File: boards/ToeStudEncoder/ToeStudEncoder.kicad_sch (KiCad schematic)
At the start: 27 parts, among them J1 Swell, J2 ISP, J3 ToeLeft, J4 ToeRight, J5 MIDI In, J8 MIDI Out, J9 Controller, Q1 BC547, U1 ATmega48-20P, U2 6N137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

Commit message: Added bypass caps to power supplies, use cheaper MAX232 IC.
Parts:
- added C3: 330nF, Capacitor_THT:C_Disc_D4.3mm_W1.9mm_P5.00mm, symbol Device:C
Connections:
- net +12V: now also C3.1
- net GND: now also C3.2
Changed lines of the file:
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@@
+	(wire
+		(pts
+			(xy 93.98 161.29) (xy 107.95 161.29)
+		)
+		(stroke
+			(width 0)
+			(type default)
+		)
+	)
 	(wire
 		(pts
@@
 		(pts
 			(xy 187.96 38.1) (xy 191.77 38.1)
+		)
+		(stroke
+			(width 0)
+			(type default)
+		)
+	)
+	(wire
+		(pts
+			(xy 93.98 162.56) (xy 93.98 161.29)
 		)
 		(stroke
@@
 	)
 	(symbol
+		(lib_id "power:GND")
+		(at 93.98 170.18 0)
+		(unit 1)
+		(exclude_from_sim no)
+		(in_bom yes)
+		(on_board yes)
+		(dnp no)
+		(fields_autoplaced yes)
+		(property "Reference" "#PWR013"
+			(at 93.98 176.53 0)
+			(effects
+				(font
+					(size 1.27 1.27)
+				)
+				(hide yes)
+			)
+		)
+		(property "Value" "GND"
+			(at 93.98 175.26 0)
+			(effects
+				(font
+					(size 1.27 1.27)
+				)
+			)
+		)
+		(property "Footprint" ""
+			(at 93.98 170.18 0)
+			(effects
+				(font
+					(size 1.27 1.27)
+				)
+				(hide yes)
+			)
+		)
+		(property "Datasheet" ""
+			(at 93.98 170.18 0)
+			(effects
+				(font
+					(size 1.27 1.27)
+				)
+				(hide yes)
+			)
+		)
+		(property "Description" "Power symbol creates a global label with name \"GND\" , ground"
+			(at 93.98 170.18 0)
+			(effects
+				(font
+					(size 1.27 1.27)
+				)
+				(hide yes)
+			)
+		)
+		(pin "1"
+		)
+		(instances
+			(project "ToeStudEncoder"
+				(path "/a0f642fd-a17d-4032-8879-54d542360da8"
+					(reference "#PWR013")
+					(unit 1)
+				)
+			)
+		)
+	)
+	(symbol
 		(lib_id "Connector_Generic:Conn_02x05_Odd_Even")
 		(at 151.13 106.68 0)
@@
 					(unit 1)
 				)
+			)
+		)
+	)
+	(symbol
+		(lib_id "Device:C")
+		(at 93.98 166.37 0)
+		(unit 1)
+		(exclude_from_sim no)
+		(in_bom yes)
+		(on_board yes)
+		(dnp no)
+		(fields_autoplaced yes)
+		(property "Reference" "C3"
+			(at 97.79 165.0999 0)
+			(effects
+				(font
+					(size 1.27 1.27)
+				)
+				(justify left)
+			)
+		)
+		(property "Value" "330nF"
+			(at 97.79 167.6399 0)
+			(effects
+				(font
+					(size 1.27 1.27)
+				)
+				(justify left)
+			)
+		)
+		(property "Footprint" "Capacitor_THT:C_Disc_D4.3mm_W1.9mm_P5.00mm"
+			(at 94.9452 170.18 0)
+			(effects
+				(font
+					(size 1.27 1.27)
+				)
+				(hide yes)
+			)
+		)
+		(property "Datasheet" "~"
+			(at 93.98 166.37 0)
+			(effects
+				(font
+					(size 1.27 1.27)
+				)
+				(hide yes)
+			)
+		)
+		(property "Description" "Unpolarized capacitor"
+			(at 93.98 166.37 0)
+			(effects
+				(font
+					(size 1.27 1.27)
+				)
+				(hide yes)
+			)
+		)
+		(pin "1"
+		)
+		(pin "2"
+		)
+		(instances
+			(project "ToeStudEncoder"
+				(path "/a0f642fd-a17d-4032-8879-54d542360da8"
+					(reference "C3")
+					(unit 1)
+				)

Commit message: Updated design rules to 0.32mm template and exported Gerber files
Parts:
- R1, R4, R5: footprint Resistor_THT:R_Axial_DIN0204_L3.6mm_D1.6mm_P2.54mm_Vertical -> Resistor_THT:R_Axial_DIN0207_L6.3mm_D2.5mm_P2.54mm_Vertical
- R2: footprint Resistor_THT:R_Axial_DIN0204_L3.6mm_D1.6mm_P7.62mm_Horizontal -> Resistor_THT:R_Axial_DIN0207_L6.3mm_D2.5mm_P2.54mm_Vertical
- R3: footprint Resistor_THT:R_Axial_DIN0204_L3.6mm_D1.6mm_P7.62mm_Horizontal -> Resistor_THT:R_Axial_DIN0207_L6.3mm_D2.5mm_P10.16mm_Horizontal
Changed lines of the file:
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@@
 			)
 		)
-		(property "Footprint" "Resistor_THT:R_Axial_DIN0204_L3.6mm_D1.6mm_P2.54mm_Vertical"
+		(property "Footprint" "Resistor_THT:R_Axial_DIN0207_L6.3mm_D2.5mm_P2.54mm_Vertical"
 			(at 239.268 62.23 90)
 			(effects
@@
 			)
 		)
-		(property "Footprint" "Resistor_THT:R_Axial_DIN0204_L3.6mm_D1.6mm_P7.62mm_Horizontal"
+		(property "Footprint" "Resistor_THT:R_Axial_DIN0207_L6.3mm_D2.5mm_P2.54mm_Vertical"
 			(at 195.58 124.968 90)
 			(effects
@@
 			)
 		)
-		(property "Footprint" "Resistor_THT:R_Axial_DIN0204_L3.6mm_D1.6mm_P2.54mm_Vertical"
+		(property "Footprint" "Resistor_THT:R_Axial_DIN0207_L6.3mm_D2.5mm_P2.54mm_Vertical"
 			(at 231.14 24.892 90)
 			(effects
@@
 			)
 		)
-		(property "Footprint" "Resistor_THT:R_Axial_DIN0204_L3.6mm_D1.6mm_P2.54mm_Vertical"
+		(property "Footprint" "Resistor_THT:R_Axial_DIN0207_L6.3mm_D2.5mm_P2.54mm_Vertical"
 			(at 189.992 30.48 90)
 			(effects
@@
 			)
 		)
-		(property "Footprint" "Resistor_THT:R_Axial_DIN0204_L3.6mm_D1.6mm_P7.62mm_Horizontal"
+		(property "Footprint" "Resistor_THT:R_Axial_DIN0207_L6.3mm_D2.5mm_P10.16mm_Horizontal"
 			(at 231.14 72.898 90)
 			(effects

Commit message: Make Toestud PS2 connectors symmetrical to avoid connection errors
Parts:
- added R6: 220, Resistor_THT:R_Axial_DIN0207_L6.3mm_D2.5mm_P10.16mm_Horizontal, symbol Device:R
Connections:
- net TXD: now also R6.1; no longer J9.4_2
- net at J9.4_1: now also J9.4_2, R6.2
- no-connect marks 16 -> 15
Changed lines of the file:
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@@
 	)
 	(junction
+		(at 215.9 137.16)
+		(diameter 0)
+		(color 0 0 0 0)
+	)
+	(junction
 		(at 157.48 49.53)
 		(diameter 0)
@@
 	)
 	(no_connect
-		(at 215.9 114.3)
-	)
-	(no_connect
 		(at 86.36 115.57)
 	)
@@
 	(wire
 		(pts
+			(xy 212.09 137.16) (xy 215.9 137.16)
+		)
+		(stroke
+			(width 0)
+			(type default)
+		)
+	)
+	(wire
+		(pts
 			(xy 73.66 57.15) (xy 73.66 59.69)
 		)
@@
 	(wire
 		(pts
+			(xy 204.47 137.16) (xy 200.66 137.16)
+		)
+		(stroke
+			(width 0)
+			(type default)
+		)
+	)
+	(wire
+		(pts
 			(xy 93.98 161.29) (xy 107.95 161.29)
 		)
@@
 	(wire
 		(pts
+			(xy 215.9 114.3) (xy 215.9 137.16)
+		)
+		(stroke
+			(width 0)
+			(type default)
+		)
+	)
+	(wire
+		(pts
 			(xy 114.3 85.09) (xy 114.3 87.63)
 		)
@@
 	(global_label "TXD"
 		(shape input)
-		(at 215.9 137.16 180)
+		(at 200.66 137.16 180)
 		(fields_autoplaced yes)
 		(effects
@@
 		)
 		(property "Intersheetrefs" "${INTERSHEET_REFS}"
-			(at 209.4677 137.16 0)
+			(at 194.2277 137.16 0)
 			(effects
 				(font
@@
 					(unit 1)
 				)
+			)
+		)
+	)
+	(symbol
+		(lib_id "Device:R")
+		(at 208.28 137.16 90)
+		(mirror x)
+		(unit 1)
+		(exclude_from_sim no)
+		(in_bom yes)
+		(on_board yes)
+		(dnp no)
+		(property "Reference" "R6"
+			(at 208.28 143.51 90)
+			(effects
+				(font
+					(size 1.27 1.27)
+				)
+			)
+		)
+		(property "Value" "220"
+			(at 208.28 140.97 90)
+			(effects
+				(font
+					(size 1.27 1.27)
+				)
+			)
+		)
+		(property "Footprint" "Resistor_THT:R_Axial_DIN0207_L6.3mm_D2.5mm_P10.16mm_Horizontal"
+			(at 208.28 135.382 90)
+			(effects
+				(font
+					(size 1.27 1.27)
+				)
+				(hide yes)
+			)
+		)
+		(property "Datasheet" "~"
+			(at 208.28 137.16 0)
+			(effects
+				(font
+					(size 1.27 1.27)
+				)
+				(hide yes)
+			)
+		)
+		(property "Description" "Resistor"
+			(at 208.28 137.16 0)
+			(effects
+				(font
+					(size 1.27 1.27)
+				)
+				(hide yes)
+			)
+		)
+		(pin "1"
+		)
+		(pin "2"
+		)
+		(instances
+			(project "ToeStudEncoder"
+				(path "/a0f642fd-a17d-4032-8879-54d542360da8"
+					(reference "R6")
+					(unit 1)
+				)

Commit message: ToeStudEncoder: Fixed mirrored PS2 pinout
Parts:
- R4: footprint Resistor_THT:R_Axial_DIN0207_L6.3mm_D2.5mm_P2.54mm_Vertical -> Resistor_THT:R_Axial_DIN0207_L6.3mm_D2.5mm_P10.16mm_Horizontal
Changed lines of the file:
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@@
 			)
 		)
-		(property "Footprint" "Resistor_THT:R_Axial_DIN0207_L6.3mm_D2.5mm_P2.54mm_Vertical"
+		(property "Footprint" "Resistor_THT:R_Axial_DIN0207_L6.3mm_D2.5mm_P10.16mm_Horizontal"
 			(at 239.268 62.23 90)
 			(effects

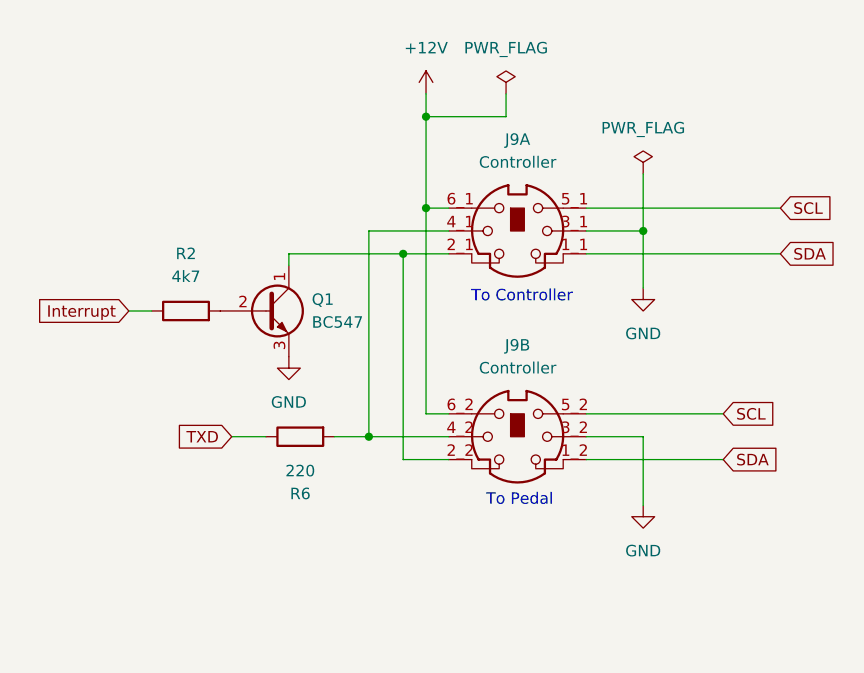
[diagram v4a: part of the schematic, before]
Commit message: Disconnected UART lines to avoid interference
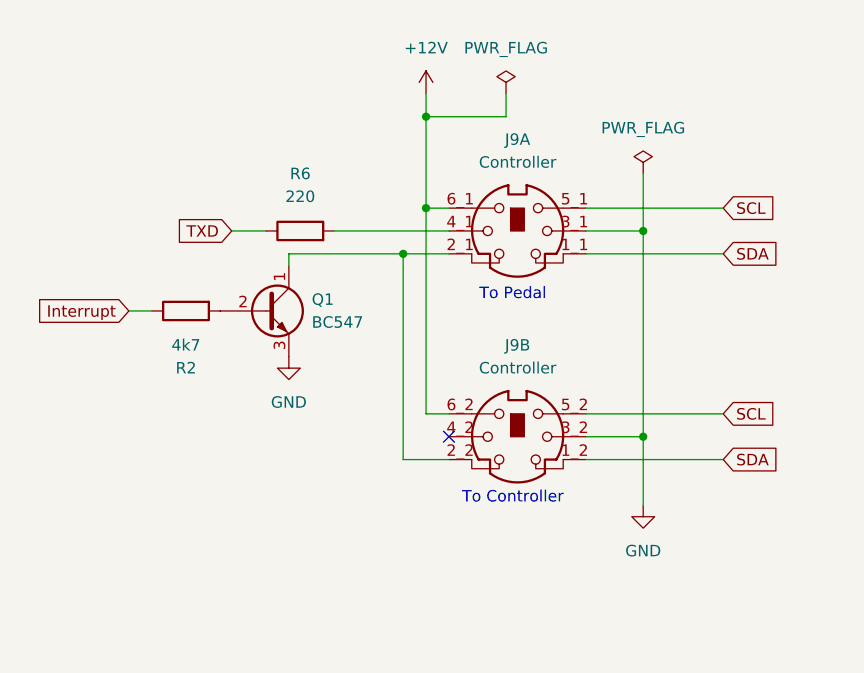
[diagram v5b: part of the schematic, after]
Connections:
- net at J9.4_1, R6.2: no longer J9.4_2
- no-connect marks 15 -> 16
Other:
- moved on the sheet: R6
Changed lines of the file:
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@@
 	)
 	(junction
-		(at 215.9 137.16)
-		(diameter 0)
-		(color 0 0 0 0)
-	)
-	(junction
 		(at 157.48 49.53)
 		(diameter 0)
@@
 	)
 	(junction
+		(at 246.38 137.16)
+		(diameter 0)
+		(color 0 0 0 0)
+	)
+	(junction
 		(at 162.56 111.76)
 		(diameter 0)
@@
 	)
 	(no_connect
+		(at 224.79 137.16)
+	)
+	(no_connect
 		(at 86.36 115.57)
 	)
@@
 	(wire
 		(pts
-			(xy 224.79 114.3) (xy 215.9 114.3)
-		)
-		(stroke
-			(width 0)
-			(type default)
-		)
-	)
-	(wire
-		(pts
 			(xy 240.03 139.7) (xy 255.27 139.7)
 		)
@@
 	(wire
 		(pts
-			(xy 71.12 135.89) (xy 71.12 139.7)
+			(xy 246.38 114.3) (xy 246.38 137.16)
 		)
 		(stroke
@@
 	(wire
 		(pts
-			(xy 157.48 39.37) (xy 157.48 35.56)
+			(xy 71.12 135.89) (xy 71.12 139.7)
 		)
 		(stroke
@@
 	(wire
 		(pts
-			(xy 219.71 139.7) (xy 224.79 139.7)
+			(xy 157.48 39.37) (xy 157.48 35.56)
 		)
 		(stroke
@@
 	(wire
 		(pts
-			(xy 212.09 137.16) (xy 215.9 137.16)
+			(xy 219.71 139.7) (xy 224.79 139.7)
 		)
 		(stroke
@@
 	(wire
 		(pts
-			(xy 246.38 114.3) (xy 246.38 120.65)
-		)
-		(stroke
-			(width 0)
-			(type default)
-		)
-	)
-	(wire
-		(pts
 			(xy 234.95 71.12) (xy 240.03 71.12)
 		)
@@
 	(wire
 		(pts
-			(xy 204.47 137.16) (xy 200.66 137.16)
+			(xy 204.47 114.3) (xy 200.66 114.3)
 		)
 		(stroke
@@
 	(wire
 		(pts
-			(xy 215.9 137.16) (xy 224.79 137.16)
+			(xy 212.09 114.3) (xy 224.79 114.3)
 		)
 		(stroke
@@
 	(wire
 		(pts
-			(xy 240.03 111.76) (xy 261.62 111.76)
+			(xy 240.03 111.76) (xy 255.27 111.76)
 		)
 		(stroke
@@
 	(wire
 		(pts
-			(xy 215.9 114.3) (xy 215.9 137.16)
-		)
-		(stroke
-			(width 0)
-			(type default)
-		)
-	)
-	(wire
-		(pts
 			(xy 114.3 85.09) (xy 114.3 87.63)
 		)
@@
 	(wire
 		(pts
-			(xy 240.03 116.84) (xy 261.62 116.84)
+			(xy 240.03 116.84) (xy 255.27 116.84)
 		)
 		(stroke
@@
 	(text "To Controller"
 		(exclude_from_sim no)
-		(at 232.918 121.666 0)
+		(at 231.902 144.018 0)
 		(effects
 			(font
@@
 	(text "To Pedal"
 		(exclude_from_sim no)
-		(at 232.664 144.272 0)
+		(at 231.902 121.412 0)
 		(effects
 			(font
@@
 	(global_label "SDA"
 		(shape input)
-		(at 261.62 116.84 0)
+		(at 255.27 116.84 0)
 		(fields_autoplaced yes)
 		(effects
@@
 		)
 		(property "Intersheetrefs" "${INTERSHEET_REFS}"
-			(at 267.6012 116.7606 0)
+			(at 261.2512 116.7606 0)
 			(effects
 				(font
@@
 	(global_label "TXD"
 		(shape input)
-		(at 200.66 137.16 180)
+		(at 200.66 114.3 180)
 		(fields_autoplaced yes)
 		(effects
@@
 		)
 		(property "Intersheetrefs" "${INTERSHEET_REFS}"
-			(at 194.2277 137.16 0)
+			(at 194.2277 114.3 0)
 			(effects
 				(font
@@
 	(global_label "SCL"
 		(shape input)
-		(at 261.62 111.76 0)
+		(at 255.27 111.76 0)
 		(fields_autoplaced yes)
 		(effects
@@
 		)
 		(property "Intersheetrefs" "${INTERSHEET_REFS}"
-			(at 267.5407 111.6806 0)
+			(at 261.1907 111.6806 0)
 			(effects
 				(font
@@
 		(lib_id "Device:R")
 		(at 195.58 123.19 90)
+		(mirror x)
 		(unit 1)
 		(exclude_from_sim no)
@@
 		(on_board yes)
 		(dnp no)
-		(fields_autoplaced yes)
 		(property "Reference" "R2"
-			(at 195.58 116.84 90)
+			(at 195.58 129.54 90)
 			(effects
 				(font
@@
 		)
 		(property "Value" "4k7"
-			(at 195.58 119.38 90)
+			(at 195.58 127 90)
 			(effects
 				(font
@@
 		)
 		(property "Footprint" "Resistor_THT:R_Axial_DIN0207_L6.3mm_D2.5mm_P2.54mm_Vertical"
-			(at 195.58 124.968 90)
+			(at 195.58 121.412 90)
 			(effects
 				(font
@@
 	(symbol
 		(lib_id "power:GND")
-		(at 246.38 120.65 0)
-		(unit 1)
-		(exclude_from_sim no)
-		(in_bom yes)
-		(on_board yes)
-		(dnp no)
-		(fields_autoplaced yes)
-		(property "Reference" "#PWR019"
-			(at 246.38 127 0)
-			(effects
-				(font
-					(size 1.27 1.27)
-				)
-				(hide yes)
-			)
-		)
-		(property "Value" "GND"
-			(at 246.38 125.73 0)
-			(effects
-				(font
-					(size 1.27 1.27)
-				)
-			)
-		)
-		(property "Footprint" ""
-			(at 246.38 120.65 0)
-			(effects
-				(font
-					(size 1.27 1.27)
-				)
-				(hide yes)
-			)
-		)
-		(property "Datasheet" ""
-			(at 246.38 120.65 0)
-			(effects
-				(font
-					(size 1.27 1.27)
-				)
-				(hide yes)
-			)
-		)
-		(property "Description" "Power symbol creates a global label with name \"GND\" , ground"
-			(at 246.38 120.65 0)
-			(effects
-				(font
-					(size 1.27 1.27)
-				)
-				(hide yes)
-			)
-		)
-		(pin "1"
-		)
-		(instances
-			(project "ToeStudEncoder"
-				(path "/a0f642fd-a17d-4032-8879-54d542360da8"
-					(reference "#PWR019")
-					(unit 1)
-				)
-			)
-		)
-	)
-	(symbol
-		(lib_id "power:GND")
 		(at 114.3 100.33 0)
 		(unit 1)
@@
 	(symbol
 		(lib_id "Device:R")
-		(at 208.28 137.16 90)
-		(mirror x)
+		(at 208.28 114.3 90)
 		(unit 1)
 		(exclude_from_sim no)
@@
 		(dnp no)
 		(property "Reference" "R6"
-			(at 208.28 143.51 90)
+			(at 208.28 107.95 90)
 			(effects
 				(font
@@
 		)
 		(property "Value" "220"
-			(at 208.28 140.97 90)
+			(at 208.28 110.49 90)
 			(effects
 				(font
@@
 		)
 		(property "Footprint" "Resistor_THT:R_Axial_DIN0207_L6.3mm_D2.5mm_P10.16mm_Horizontal"
-			(at 208.28 135.382 90)
+			(at 208.28 116.078 90)
 			(effects
 				(font
@@
 		)
 		(property "Datasheet" "~"
-			(at 208.28 137.16 0)
+			(at 208.28 114.3 0)
 			(effects
 				(font
@@
 		)
 		(property "Description" "Resistor"
-			(at 208.28 137.16 0)
+			(at 208.28 114.3 0)
 			(effects
 				(font
